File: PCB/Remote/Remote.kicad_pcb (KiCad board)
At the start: 2 copper layers, 70 x 70 mm, 90 parts, among them J1 LCD, J2 DC, J3 TEMP, J4 LCD, J5 Reset, J6 USB-C-Socket-H, J7 TC2030-USB-NL-DS, T1 T3902_MEMS_Mic, U1 ESP32-S3-MINI-1, U2 SCD41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

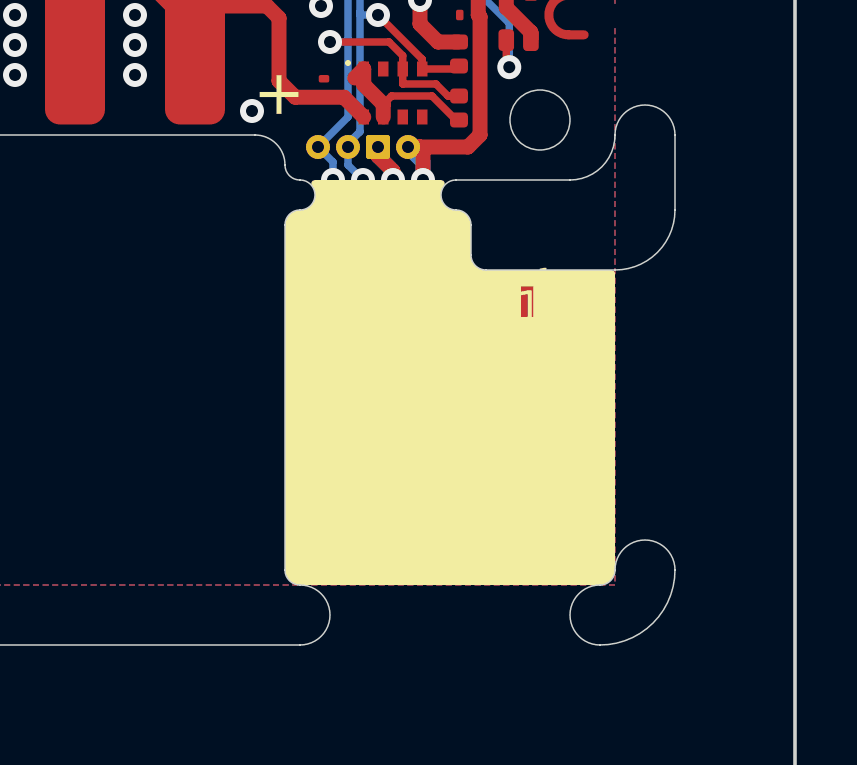
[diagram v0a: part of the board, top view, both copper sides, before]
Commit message: Re render and new knob
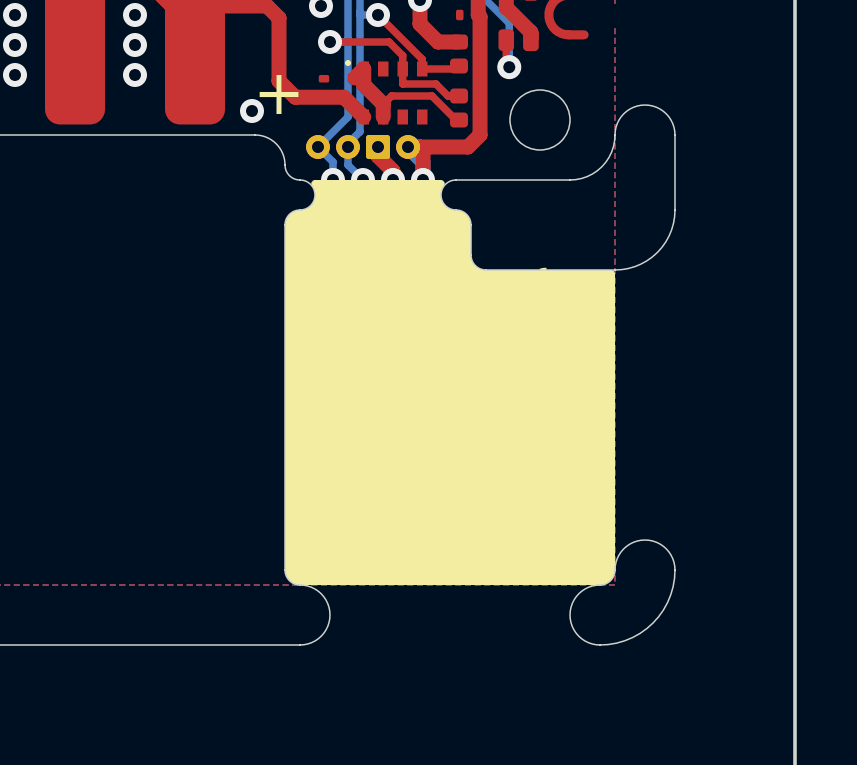
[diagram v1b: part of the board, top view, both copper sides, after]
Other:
- board text removed: "1"

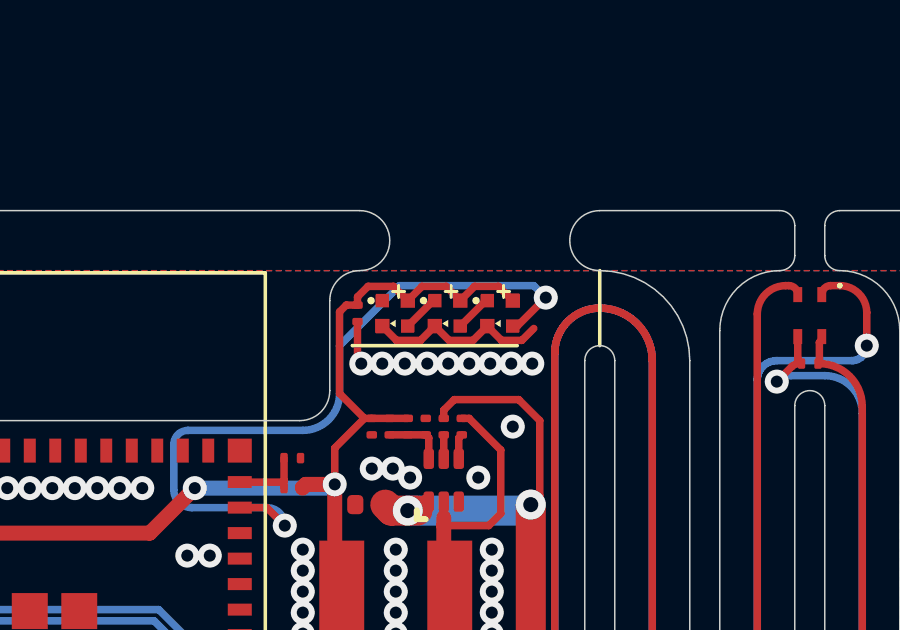
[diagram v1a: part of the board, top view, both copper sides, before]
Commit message: New LED
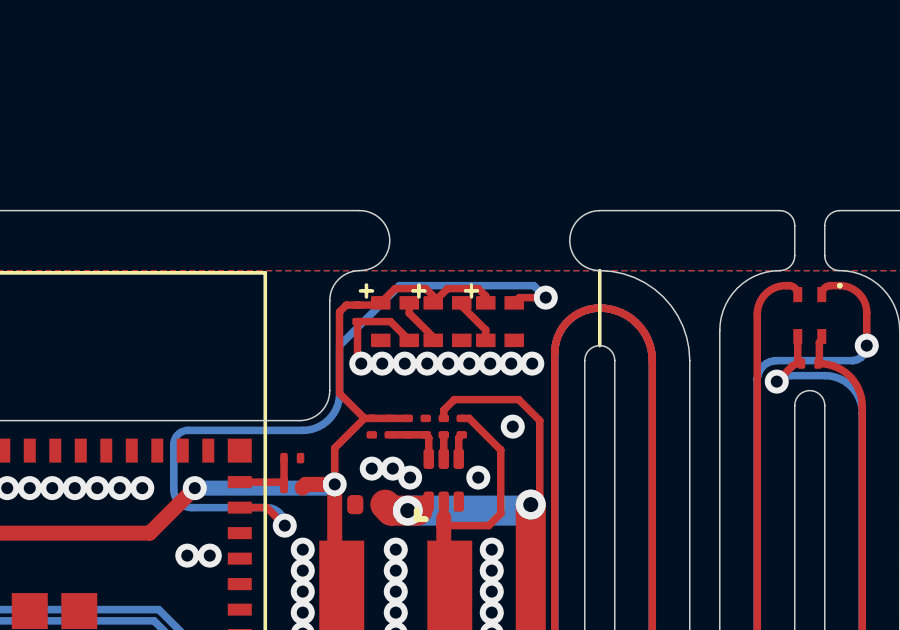
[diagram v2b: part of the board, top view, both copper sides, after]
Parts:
- D4, D5, D6: footprint RevK:SMD1010-Side2 -> RevK:SMD1615
- moved D4 0.28 mm to (105.7, 76.7), turned to 90 degrees
- moved D5 0.28 mm to (103.9, 76.7), turned to 90 degrees
- moved D6 0.28 mm to (102.2, 76.7), turned to 90 degrees
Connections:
- D4 pad 1: Net-(D4-O) -> GND
- D4 pad 2: +3.3V -> LED
- D4 pad 3: GND -> +3.3V
- D4 pad 4: LED -> Net-(D4-O)
- D5 pad 1: Net-(D5-O) -> GND
- D5 pad 2: +3.3V -> Net-(D4-O)
- D5 pad 3: GND -> +3.3V
- D5 pad 4: Net-(D4-O) -> Net-(D5-I)
- D6 pad 1: unconnected-(D6-O-Pad1) -> GND
- D6 pad 2: +3.3V -> Net-(D5-I)
- D6 pad 3: GND -> +3.3V
- D6 pad 4: Net-(D5-O) -> unconnected-(D6-O-Pad4)
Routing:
- net GND: track 95.4 -> 91.2 mm
- net Net-(D5-I): track 0.00 -> 1.58 mm
- net +3.3V: track 262.7 -> 261.5 mm
- net Net-(D5-O): track 1.20 -> 0.00 mm

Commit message: Library update
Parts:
- U1: value ESP32-S3-MINI-1 -> ESP32-S3-MINI-1-N4R2

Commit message: Tweaks, but cases look wrong
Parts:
- U9: footprint RevK:SOT-563 -> RevK:SOT-5x3-6
- moved J2 0.25 mm to (88.8, 104.5)
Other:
- board text added: "E"

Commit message: Library update
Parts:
- U1: value ESP32-S3-MINI-1-N4R2 -> ESP32-S3-MINI-1

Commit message: Improved case design
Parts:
- D4: value XL-1010RGBC-WS2812B -> XL-1615RGBC-2812B; footprint RevK:SMD1615 -> RevK:SMD1615-Side
- D5, D6: footprint RevK:SMD1615 -> RevK:SMD1615-Side
